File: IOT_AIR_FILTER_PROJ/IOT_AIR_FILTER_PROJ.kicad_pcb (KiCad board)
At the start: 2 copper layers, 40 x 40 mm, 21 parts, among them J1 Conn_ARM_SWD_TagConnect_TC203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, J2 Conn_01x02_Socket, J3 Conn_01x04_Pin, J4 Conn_01x04_Pin, J5 Conn_01x04_Pin, J6 Conn_01x04_Pin, J7 Conn_01x04_Pin, U1 PIC16F18124-I/SL, U2 AMS1117-5.0, U3 ADG419BR

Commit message: minor changes to schematic, component selection and layout
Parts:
- added C6: 47uF, Capacitor_SMD:CP_Elec_4x3, F.Cu at (130.2, 55.5)
- added R4: 4.7k, Resistor_SMD:R_0805_2012Metric, F.Cu at (111.2, 65.0)
- added R5: 4.7k, Resistor_SMD:R_0805_2012Metric, F.Cu at (109.3, 77.6)
- C1: value 22uF -> 47uF; footprint Capacitor_SMD:C_1210_3225Metric -> Capacitor_SMD:CP_Elec_4x3
- C2: value 22uF -> 100nF
- moved C2 7.10 mm to (134.2, 60.2), turned to 0 degrees
- moved C1 1.03 mm to (117.2, 56.5)
- moved J7 0.87 mm to (134.8, 72.2)
- moved J5 0.86 mm to (128.8, 85.8)
- moved J6 0.86 mm to (116.8, 85.8)
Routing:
- net +5V: track 77.2 -> 92.1 mm, vias 4 -> 5
- net Net-(U1-RC5): track 0.00 -> 7.41 mm
- net GND: track 0.00 -> 7.37 mm, vias 0 -> 33
- net Net-(D1-A): track 0.00 -> 1.85 mm
- net /SCL: track 38.6 -> 36.9 mm
- net /RX: track 17.1 -> 15.8 mm
- net RST: track 19.3 -> 20.5 mm
- net /TX: track 13.5 -> 12.4 mm
- net Net-(J4-Pin_3): track 8.59 -> 9.41 mm

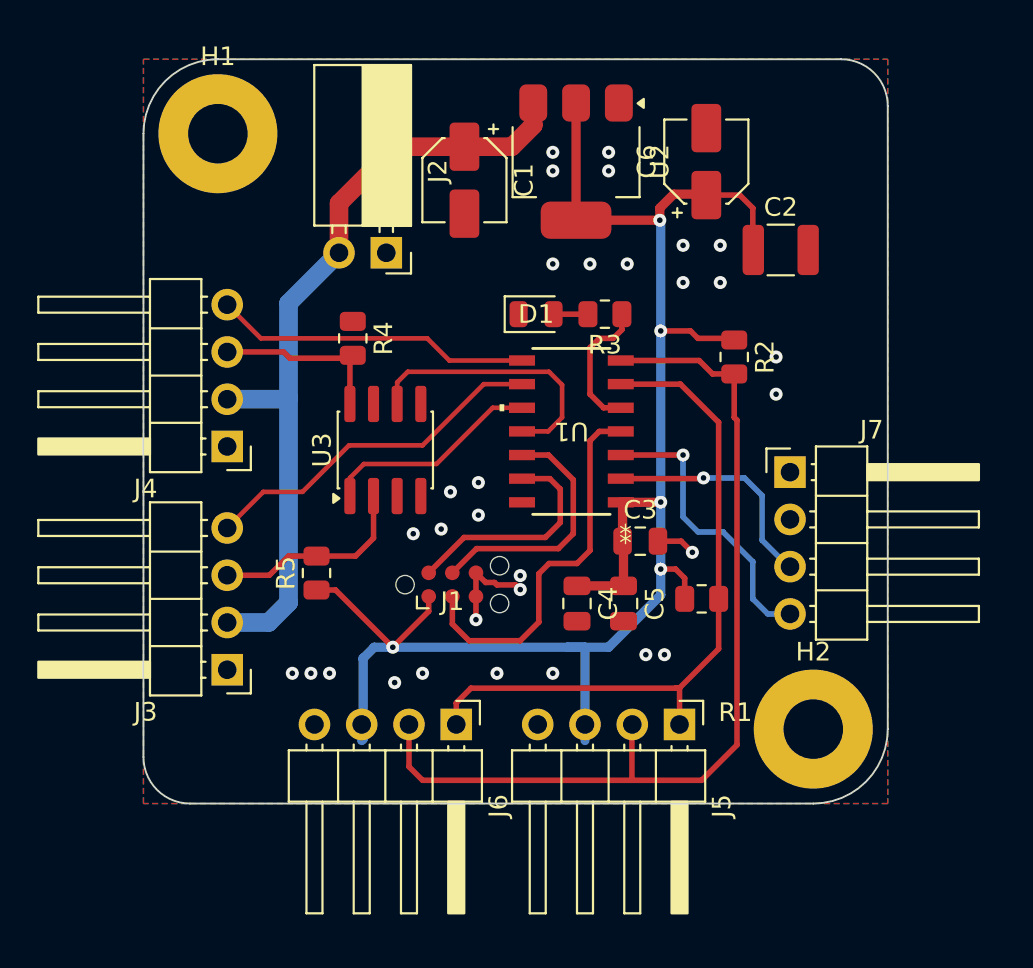
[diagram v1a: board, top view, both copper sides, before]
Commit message: added schematics/layout/manufacturing files. Also initial FW for IOT sensor
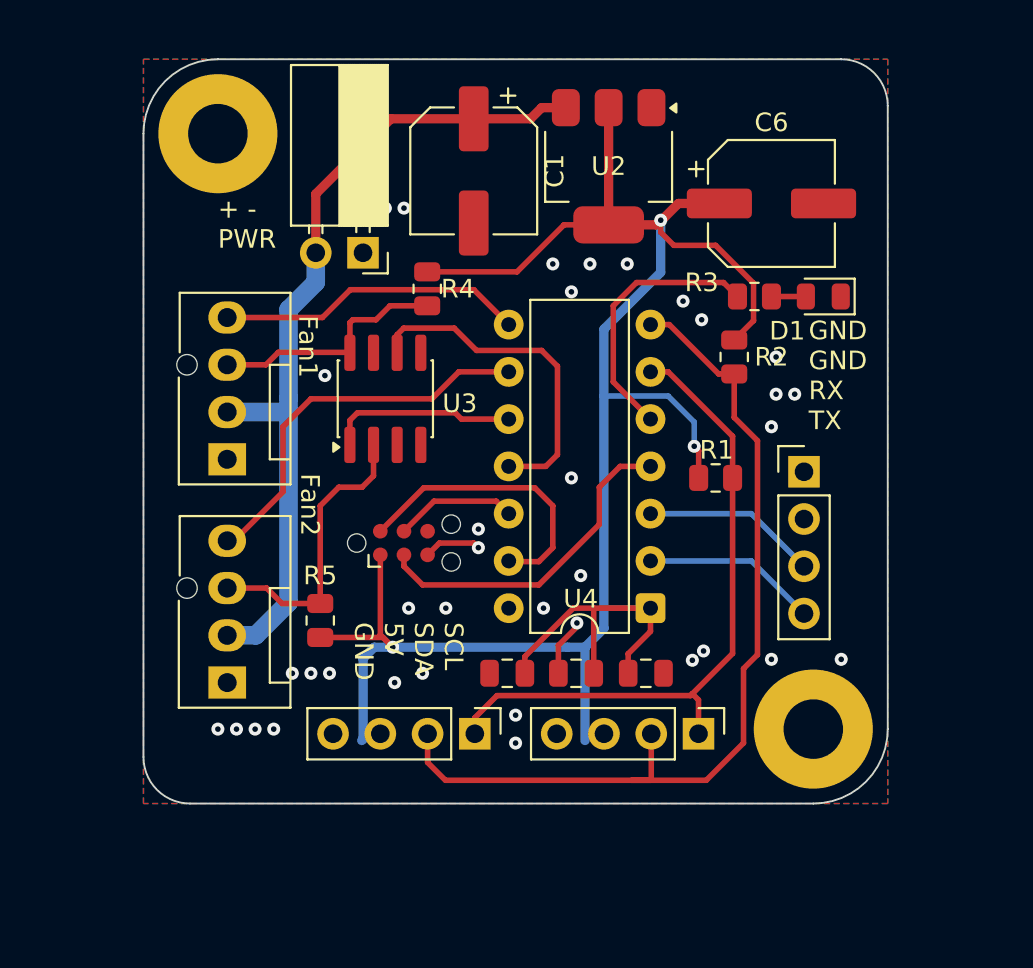
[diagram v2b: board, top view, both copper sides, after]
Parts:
- removed C2: 100nF, Capacitor_SMD:C_1210_3225Metric
- removed U1: PIC16F18124-I/SL, PIC16F18124:PIC16F18124_SOIC14_SL_MCH
- added U4: PIC16F18124, Package_DIP:DIP-14_W7.62mm, F.Cu at (127.2, 79.5)
- C1, C6: footprint Capacitor_SMD:CP_Elec_4x3 -> Capacitor_SMD:CP_Elec_6.3x5.4
- J3, J4: footprint Connector_PinHeader_2.54mm:PinHeader_1x04_P2.54mm_Horizontal -> Connector:FanPinHeader_1x04_P2.54mm_Vertical
- J5, J6, J7: footprint Connector_PinHeader_2.54mm:PinHeader_1x04_P2.54mm_Horizontal -> Connector_PinHeader_2.54mm:PinHeader_1x04_P2.54mm_Vertical
- R3: value 432 -> 470
- moved D1 15.5 mm to (136.5, 62.8), turned to 180 degrees
- moved R3 8.09 mm to (132.8, 62.8), turned to 0 degrees
- moved C5 7.29 mm to (119.5, 83.0), turned to 180 degrees
- moved C3 7.11 mm to (127.0, 83.0)
- moved R1 6.54 mm to (130.8, 72.5)
- moved R4 4.81 mm to (115.2, 62.3)
- moved C6 4.16 mm to (133.8, 57.8), turned to 0 degrees
- moved C4 3.75 mm to (123.2, 83.0), turned to 180 degrees
- moved J1 3.43 mm to (114.0, 76.0)
- moved U3 2.75 mm to (113.0, 68.2)
- moved R5 2.56 mm to (109.5, 80.2)
- moved U2 1.77 mm to (125.0, 55.8)
- moved J2 1.25 mm to (111.8, 60.4)
- moved J5 1.14 mm to (129.8, 86.2)
- moved J6 1.12 mm to (117.8, 86.2)
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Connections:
- J1 pad 6: GND -> unconnected-(J1-SWO-Pad6)
- J7 pad 3: /TX -> /RX
- J7 pad 4: /RX -> /TX
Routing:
- net +5V: track 92.1 -> 116.8 mm, vias 5 -> 3
- net Net-(U4-RC5): track 7.41 -> 14.4 mm
- net SWCLK: track 13.6 -> 6.58 mm
- net /RX: track 15.8 -> 9.42 mm, vias 1 -> 0
- net Net-(J3-Pin_3): track 11.0 -> 15.8 mm
- net Net-(J4-Pin_3): track 9.41 -> 13.0 mm
- net /FAN_TACH_SELECT: track 14.8 -> 18.2 mm
- net SWDIO: track 12.3 -> 15.6 mm
- net /TX: track 12.4 -> 9.42 mm, vias 1 -> 0
- net RST: track 20.5 -> 18.1 mm
- net PWM11: track 19.0 -> 20.9 mm
- net /T1CKI: track 11.8 -> 10.2 mm
- net +12V: track 43.0 -> 44.6 mm
- net GND: track 7.37 -> 6.21 mm, vias 33 -> 36
- net /SCL: track 36.9 -> 36.0 mm
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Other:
- board text added: "+ - PWR"
- board text added: "Fan1"
- board text added: "Fan2"
- board text added: "GND GND RX TX"
- board text added: "SCL SDA 5V GND"

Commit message: added raspberry pi stuff
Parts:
- removed J1: Conn_ARM_SWD_TagConnect_TC2030-NL, Connector:Tag-Connect_TC2030-IDC-NL_2x03_P1.27mm_Vertical
- added J8: Conn_02x03_Counter_Clockwise, Connector_PinSocket_2.54mm:PinSocket_2x03_P2.54mm_Vertical, F.Cu at (113.4, 78.9)
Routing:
- net SWDIO: track 15.6 -> 4.49 mm
- net GND: track 6.21 -> 3.12 mm
- net +5V: track 116.8 -> 114.3 mm
- net RST: track 18.1 -> 15.7 mm
- net SWCLK: track 6.58 -> 4.49 mm
